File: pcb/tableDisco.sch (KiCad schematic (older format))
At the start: 7 parts, among them J1 Mic Connection, J2 LED Connection, J3 Mode Switch, J5 Power Connection, U1 WeMos_D1_mini

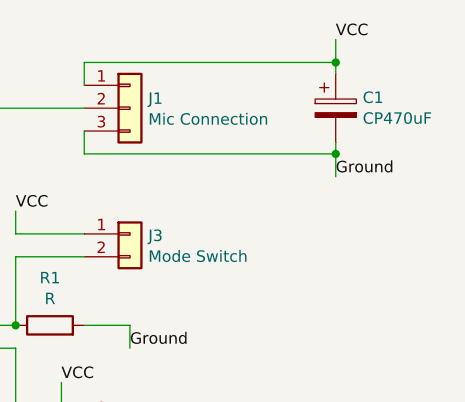
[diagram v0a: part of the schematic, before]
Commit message: Fix capacitor value
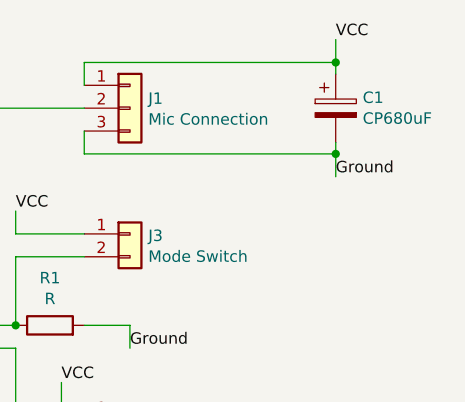
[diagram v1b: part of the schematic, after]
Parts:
- C1: value CP470uF -> CP680uF
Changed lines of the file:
@@
 P 4350 950
 F 0 "C1" H 4468 996 50  0000 L CNN
-F 1 "CP470uF" H 4468 905 50  0000 L CNN
+F 1 "CP680uF" H 4468 905 50  0000 L CNN
 F 2 "Capacitor_THT:CP_Radial_D6.3mm_P2.50mm" H 4388 800 50  0001 C CNN
 F 3 "~" H 4350 950 50  0001 C CNN
